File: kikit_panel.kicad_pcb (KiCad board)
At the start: 4 copper layers, 56 x 47 mm, 297 parts, among them J1 Conn_01x01, J10 Conn_01x01, J11 Conn_01x01, J12 Conn_01x01, J13 Conn_01x01, J14 Conn_01x01, J15 Conn_01x01, J16 Conn_01x01, J17 Conn_Coaxial, J2 Conn_01x01, J3 Conn_01x01, J4 Conn_01x01, J5 Conn_01x01, J6 Conn_01x01, J7 Conn_01x01, J8 Conn_01x01, J9 Conn_01x01, U1 SX1280IMLTRT, U2 2450FM07D0034T, X1 52.000 MHz

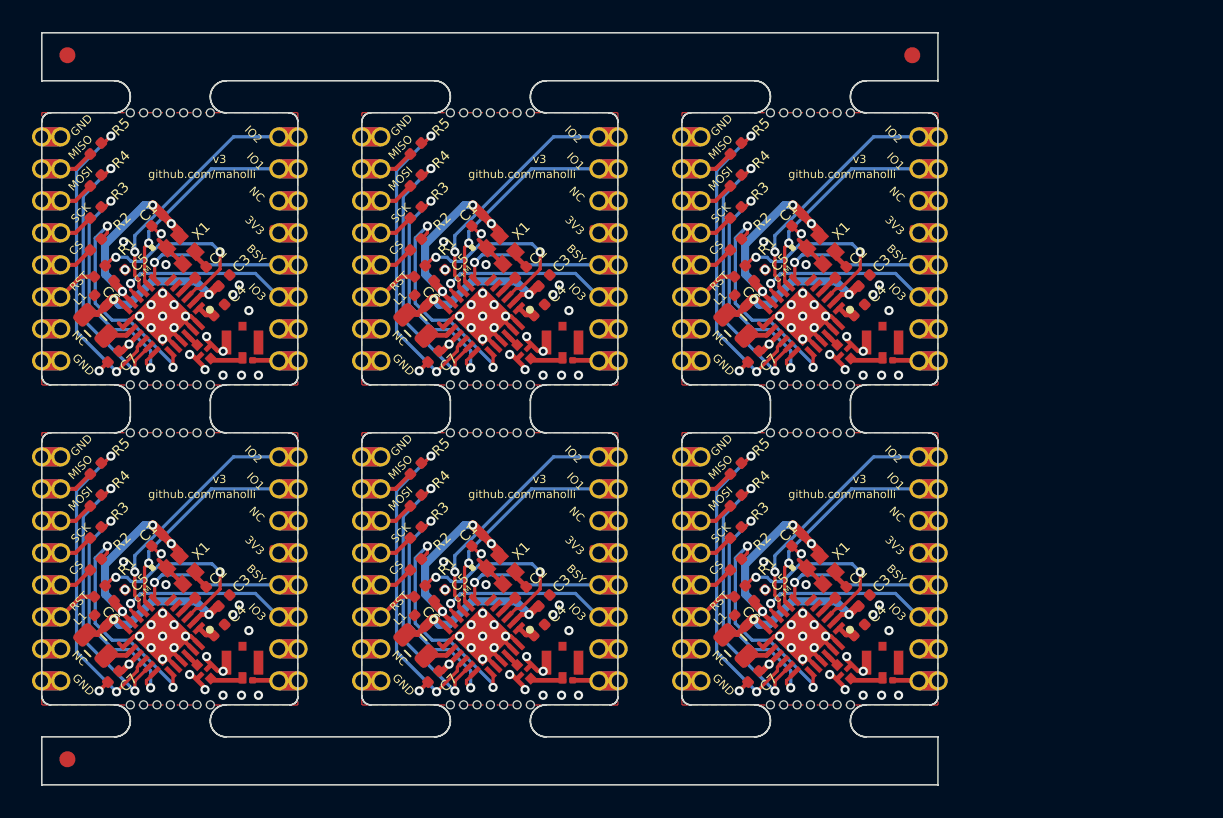
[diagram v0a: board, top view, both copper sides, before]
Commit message: panelized just in case
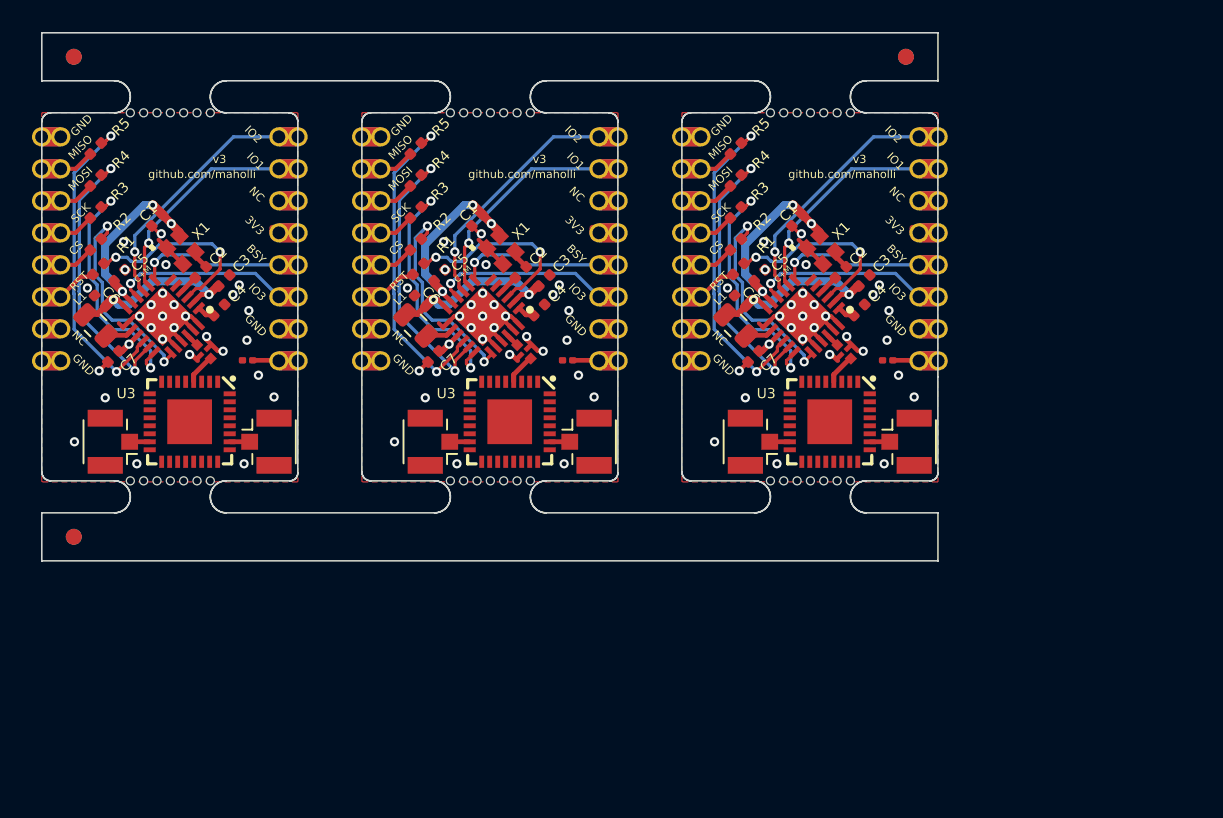
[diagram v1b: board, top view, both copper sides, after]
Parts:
- removed the C1 at (62.2, 46.7)
- removed the C1 at (42.2, 46.7)
- removed the C1 at (22.2, 46.7)
- removed the C2 at (64.9, 50.0)
- removed the C2 at (24.9, 50.0)
- removed the C2 at (44.9, 50.0)
- removed the C3 at (66.4, 50.5)
- removed the C3 at (46.4, 50.5)
- removed the C3 at (26.4, 50.5)
- removed the C4 at (26.1, 52.3)
- removed the C4 at (46.1, 52.3)
- removed the C4 at (66.1, 52.3)
- removed the C5 at (59.9, 50.2)
- removed the C5 at (39.9, 50.2)
- removed the C5 at (19.9, 50.2)
- removed the C6 at (38.6, 51.7)
- removed the C6 at (18.6, 51.7)
- removed the C6 at (18.6, 31.7)
- removed the C6 at (58.6, 31.7)
- removed the C6 at (58.6, 51.7)
- removed the C6 at (38.6, 31.7)
- removed the C7 at (59.5, 55.2)
- removed the C7 at (39.5, 55.2)
- removed the C7 at (19.5, 55.2)
- removed the J1 at (35.0, 41.5)
- removed the J1 at (15.0, 41.5)
- removed the J1 at (55.0, 41.5)
- removed the J10 at (31.0, 53.5)
- removed the J10 at (71.0, 53.5)
- removed the J10 at (51.0, 53.5)
- removed the J11 at (51.0, 51.5)
- removed the J11 at (31.0, 51.5)
- removed the J11 at (71.0, 51.5)
- removed the J12 at (51.0, 49.5)
- removed the J12 at (71.0, 49.5)
- removed the J12 at (31.0, 49.5)
- removed the J13 at (31.0, 47.5)
- removed the J13 at (51.0, 47.5)
- removed the J13 at (71.0, 47.5)
- removed the J14 at (51.0, 45.5)
- removed the J14 at (71.0, 45.5)
- removed the J14 at (31.0, 45.5)
- removed the J15 at (51.0, 43.5)
- removed the J15 at (71.0, 43.5)
- removed the J15 at (31.0, 43.5)
- removed the J16 at (31.0, 41.5)
- removed the J16 at (51.0, 41.5)
- removed the J16 at (71.0, 41.5)
- removed the J17 at (27.5, 34.4)
- removed the J17 at (27.5, 54.4)
- removed the J17 at (47.5, 34.4)
- removed the J17 at (67.5, 34.4)
- removed the J17 at (47.5, 54.4)
- removed the J17 at (67.5, 54.4)
- removed the J2 at (15.0, 43.5)
- removed the J2 at (35.0, 43.5)
- removed the J2 at (55.0, 43.5)
- removed the J3 at (55.0, 45.5)
- removed the J3 at (35.0, 45.5)
- removed the J3 at (15.0, 45.5)
- removed the J4 at (15.0, 47.5)
- removed the J4 at (35.0, 47.5)
- removed the J4 at (55.0, 47.5)
- removed the J5 at (55.0, 49.5)
- removed the J5 at (35.0, 49.5)
- removed the J5 at (15.0, 49.5)
- removed the J6 at (35.0, 51.5)
- removed the J6 at (15.0, 51.5)
- removed the J6 at (55.0, 51.5)
- removed the J7 at (55.0, 53.5)
- removed the J7 at (15.0, 53.5)
- removed the J7 at (35.0, 53.5)
- removed the J8 at (35.0, 55.5)
- removed the J8 at (15.0, 55.5)
- removed the J8 at (55.0, 55.5)
- removed the J9 at (51.0, 55.5)
- removed the J9 at (31.0, 55.5)
- removed the J9 at (71.0, 55.5)
- removed the L1 at (38.4, 53.3)
- removed the L1 at (58.4, 53.3)
- removed the L1 at (18.4, 53.3)
- removed the R1 at (38.6, 49.9)
- removed the R1 at (58.6, 29.9)
- removed the R1 at (58.6, 49.9)
- removed the R1 at (38.6, 29.9)
- removed the R1 at (18.6, 29.9)
- removed the R1 at (18.6, 49.9)
- removed the R2 at (18.4, 48.2)
- removed the R2 at (58.4, 48.2)
- removed the R2 at (38.4, 48.2)
- removed the R3 at (58.4, 46.2)
- removed the R3 at (18.4, 46.2)
- removed the R3 at (38.4, 46.2)
- removed the R4 at (58.4, 44.2)
- removed the R4 at (18.4, 44.2)
- removed the R4 at (38.4, 44.2)
- removed the R5 at (18.4, 42.2)
- removed the R5 at (38.4, 42.2)
- removed the R5 at (58.4, 42.2)
- removed the R6 at (67.9, 55.5)
- removed the R6 at (27.9, 55.5)
- removed the R6 at (47.9, 55.5)
- removed the REF** at (62.2, 40.0)
- removed the REF** at (63.0, 37.0)
- removed the REF** at (60.5, 57.0)
- removed the REF** at (23.0, 40.0)
- removed the REF** at (43.9, 40.0)
- removed the REF** at (43.0, 57.0)
- removed the REF** at (41.4, 40.0)
- removed the REF** at (61.4, 37.0)
- removed the REF** at (23.9, 40.0)
- removed the REF** at (63.9, 40.0)
- removed the REF** at (40.5, 40.0)
- removed the REF** at (63.0, 40.0)
- removed the REF** at (22.2, 37.0)
- removed the REF** at (25.5, 57.0)
- removed the REF** at (20.5, 40.0)
- removed the REF** at (65.5, 40.0)
- removed the REF** at (61.4, 57.0)
- removed the REF** at (62.2, 37.0)
- removed the REF** at (24.7, 40.0)
- removed the REF** at (23.9, 37.0)
- removed the REF** at (44.7, 57.0)
- removed the REF** at (23.9, 57.0)
- removed the REF** at (24.7, 37.0)
- removed the REF** at (45.5, 37.0)
- removed the REF** at (60.5, 37.0)
- removed the REF** at (63.0, 57.0)
- removed the REF** at (42.2, 57.0)
- removed the REF** at (43.0, 40.0)
- removed the REF** at (64.7, 37.0)
- removed the REF** at (23.0, 37.0)
- removed the REF** at (25.5, 37.0)
- removed the REF** at (64.7, 40.0)
- removed the REF** at (64.7, 57.0)
- removed the REF** at (21.4, 40.0)
- removed the REF** at (24.7, 57.0)
- removed the REF** at (62.2, 57.0)
- removed the REF** at (20.5, 37.0)
- removed the REF** at (43.9, 57.0)
- removed the REF** at (45.5, 40.0)
- removed the REF** at (40.5, 37.0)
- removed the REF** at (25.5, 40.0)
- removed the REF** at (65.5, 57.0)
- removed the REF** at (41.4, 37.0)
- removed the REF** at (23.0, 57.0)
- removed the REF** at (40.5, 57.0)
- removed the REF** at (21.4, 57.0)
- removed the REF** at (60.5, 40.0)
- removed the REF** at (16.6, 60.4)
- removed the REF** at (65.5, 37.0)
- removed the REF** at (44.7, 40.0)
- removed the REF** at (44.7, 37.0)
- removed the REF** at (45.5, 57.0)
- removed the REF** at (61.4, 40.0)
- removed the REF** at (21.4, 37.0)
- removed the REF** at (16.6, 16.4)
- removed the REF** at (69.4, 16.4)
- removed the REF** at (63.9, 37.0)
- removed the REF** at (43.0, 37.0)
- removed the REF** at (22.2, 40.0)
- removed the REF** at (41.4, 57.0)
- removed the REF** at (22.2, 57.0)
- removed the REF** at (43.9, 37.0)
- removed the REF** at (63.9, 57.0)
- removed the REF** at (42.2, 37.0)
- removed the REF** at (20.5, 57.0)
- removed the REF** at (42.2, 40.0)
- removed the Ref** at (42.8, 44.8)
- removed the Ref** at (62.8, 44.8)
- removed the Ref** at (22.8, 44.8)
- removed the U1 at (62.6, 52.7)
- removed the U1 at (42.6, 52.7)
- removed the U1 at (22.5, 52.7)
- removed the U2 at (25.1, 54.9)
- removed the U2 at (65.1, 54.9)
- removed the U2 at (45.1, 54.9)
- removed the X1 at (63.7, 48.6)
- removed the X1 at (23.7, 48.6)
- removed the X1 at (43.7, 48.6)
- added C6: 470nF, Capacitor_SMD:C_0402_1005Metric, F.Cu at (18.6, 31.8)
- added C6: 470nF, Capacitor_SMD:C_0402_1005Metric, F.Cu at (38.6, 31.8)
- added C6: 470nF, Capacitor_SMD:C_0402_1005Metric, F.Cu at (58.6, 31.8)
- added J17: u.FL, Connector_Coaxial:U.FL_Hirose_U.FL-R-SMT-1_Vertical, F.Cu at (59.4, 40.6)
- added J17: u.FL, Connector_Coaxial:U.FL_Hirose_U.FL-R-SMT-1_Vertical, F.Cu at (39.4, 40.6)
- added J17: u.FL, Connector_Coaxial:U.FL_Hirose_U.FL-R-SMT-1_Vertical, F.Cu at (19.4, 40.6)
- added J18: u.FL, Connector_Coaxial:U.FL_Hirose_U.FL-R-SMT-1_Vertical, F.Cu at (29.0, 40.6)
- added J18: u.FL, Connector_Coaxial:U.FL_Hirose_U.FL-R-SMT-1_Vertical, F.Cu at (69.0, 40.6)
- added J18: u.FL, Connector_Coaxial:U.FL_Hirose_U.FL-R-SMT-1_Vertical, F.Cu at (49.0, 40.6)
- added R1: 1k, Resistor_SMD:R_0402_1005Metric, F.Cu at (58.5, 29.8)
- added R1: 1k, Resistor_SMD:R_0402_1005Metric, F.Cu at (38.5, 29.8)
- added R1: 1k, Resistor_SMD:R_0402_1005Metric, F.Cu at (18.5, 29.8)
- added REF**: NPTH, NPTH, F.Cu at (21.4, 43.0)
- added REF**: NPTH, NPTH, F.Cu at (61.4, 43.0)
- added REF**: NPTH, NPTH, F.Cu at (63.9, 43.0)
- added REF**: NPTH, NPTH, F.Cu at (42.2, 43.0)
- added REF**: NPTH, NPTH, F.Cu at (62.2, 43.0)
- added REF**: NPTH, NPTH, F.Cu at (64.7, 43.0)
- added REF**: Fiducial, Fiducial, F.Cu at (17.0, 16.5)
- added REF**: NPTH, NPTH, F.Cu at (41.4, 43.0)
- added REF**: NPTH, NPTH, F.Cu at (24.7, 43.0)
- added REF**: NPTH, NPTH, F.Cu at (44.7, 43.0)
- added REF**: NPTH, NPTH, F.Cu at (23.0, 43.0)
- added REF**: NPTH, NPTH, F.Cu at (22.2, 43.0)
- added REF**: NPTH, NPTH, F.Cu at (60.5, 43.0)
- added REF**: NPTH, NPTH, F.Cu at (23.9, 43.0)
- added REF**: NPTH, NPTH, F.Cu at (40.5, 43.0)
- added REF**: NPTH, NPTH, F.Cu at (45.5, 43.0)
- added REF**: Fiducial, Fiducial, F.Cu at (69.0, 16.5)
- added REF**: NPTH, NPTH, F.Cu at (20.5, 43.0)
- added REF**: NPTH, NPTH, F.Cu at (25.5, 43.0)
- added REF**: NPTH, NPTH, F.Cu at (43.0, 43.0)
- added REF**: Fiducial, Fiducial, F.Cu at (17.0, 46.5)
- added REF**: Fiducial, Fiducial, B.Cu at (17.0, 46.5)
- added REF**: Fiducial, Fiducial, B.Cu at (69.0, 16.5)
- added REF**: Fiducial, Fiducial, B.Cu at (17.0, 16.5)
- added REF**: NPTH, NPTH, F.Cu at (43.9, 43.0)
- added REF**: NPTH, NPTH, F.Cu at (65.5, 43.0)
- added REF**: NPTH, NPTH, F.Cu at (63.0, 43.0)
- added U3: EP2W+, custom-footprints:QFN32-5X5MM, F.Cu at (24.2, 39.3)
- added U3: EP2W+, custom-footprints:QFN32-5X5MM, F.Cu at (64.2, 39.3)
- added U3: EP2W+, custom-footprints:QFN32-5X5MM, F.Cu at (44.2, 39.3)
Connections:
- net Board_0-Net-(X1-Pad3) renamed Board_0-Net-(C2-Pad2)
- net Board_1-Net-(X1-Pad3) renamed Board_1-Net-(C2-Pad2)
- net Board_2-Net-(X1-Pad3) renamed Board_2-Net-(C2-Pad2)
- R6 pad 1: Board_1-Net-(J17-Pad1) -> Board_1-unconnected-(R6-Pad1)
- R6 pad 1: Board_0-Net-(J17-Pad1) -> Board_0-unconnected-(R6-Pad1)
- R6 pad 1: Board_2-Net-(J17-Pad1) -> Board_2-unconnected-(R6-Pad1)
- U2 pad 3: Board_2-Net-(J17-Pad1) -> Board_2-Net-(U2-Pad3)
- U2 pad 3: Board_0-Net-(J17-Pad1) -> Board_0-Net-(U2-Pad3)
- U2 pad 3: Board_1-Net-(J17-Pad1) -> Board_1-Net-(U2-Pad3)
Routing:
- net Board_5-+3V3: track 24.2 -> 0.00 mm, vias 4 -> 0
- net Board_4-+3V3: track 24.2 -> 0.00 mm, vias 4 -> 0
- net Board_3-+3V3: track 24.2 -> 0.00 mm, vias 4 -> 0
- net Board_5-Net-(R5-Pad2): track 20.0 -> 0.00 mm, vias 2 -> 0
- net Board_4-Net-(R5-Pad2): track 20.0 -> 0.00 mm, vias 2 -> 0
- net Board_3-Net-(R5-Pad2): track 20.0 -> 0.00 mm, vias 2 -> 0
- net Board_5-Net-(R4-Pad2): track 17.4 -> 0.00 mm, vias 2 -> 0
- net Board_4-Net-(R4-Pad2): track 17.4 -> 0.00 mm, vias 2 -> 0
- net Board_3-Net-(R4-Pad2): track 17.4 -> 0.00 mm, vias 2 -> 0
- net Board_5-SX_DIO2: track 15.3 -> 0.00 mm, vias 1 -> 0
- net Board_4-SX_DIO2: track 15.3 -> 0.00 mm, vias 1 -> 0
- net Board_3-SX_DIO2: track 15.3 -> 0.00 mm, vias 1 -> 0
- net Board_5-Net-(R3-Pad2): track 15.2 -> 0.00 mm, vias 2 -> 0
- net Board_3-Net-(R3-Pad2): track 15.2 -> 0.00 mm, vias 2 -> 0
- net Board_4-Net-(R3-Pad2): track 15.2 -> 0.00 mm, vias 2 -> 0
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- removed copper zone on F.Cu, net Board_3-GND
- removed copper zone on In1.Cu, net Board_3-GND
- removed copper zone on In2.Cu, net Board_3-GND
- removed copper zone on F.Cu, net Board_4-GND
- removed copper zone on In1.Cu, net Board_4-GND
- removed copper zone on In2.Cu, net Board_4-GND
- removed copper zone on F.Cu, net Board_5-GND
- removed copper zone on In1.Cu, net Board_5-GND
- removed copper zone on In2.Cu, net Board_5-GND
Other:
- board size 56 x 47 mm -> 56 x 33 mm

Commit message: back to single antenna
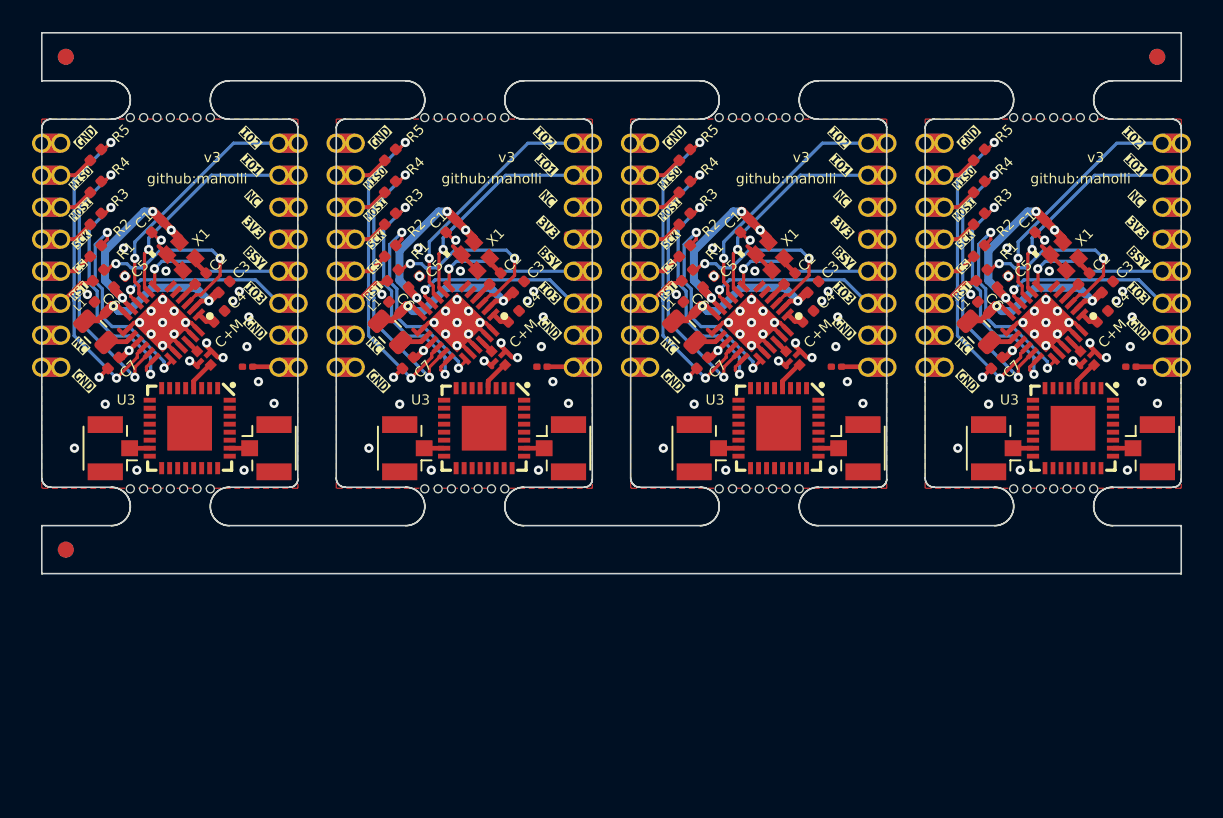
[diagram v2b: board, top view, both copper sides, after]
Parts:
- removed the C1 at (62.2, 26.7)
- removed the C1 at (22.2, 26.7)
- removed the C1 at (42.2, 26.7)
- removed the C2 at (44.9, 30.0)
- removed the C2 at (64.9, 30.0)
- removed the C2 at (24.9, 30.0)
- removed the C3 at (66.4, 30.5)
- removed the C3 at (46.4, 30.5)
- removed the C3 at (26.4, 30.5)
- removed the C4 at (26.1, 32.3)
- removed the C4 at (66.1, 32.3)
- removed the C4 at (46.1, 32.3)
- removed the C5 at (39.9, 30.2)
- removed the C5 at (59.9, 30.2)
- removed the C5 at (19.9, 30.2)
- removed the C6 at (18.6, 31.8)
- removed the C6 at (38.6, 31.8)
- removed the C6 at (58.6, 31.8)
- removed the C7 at (59.5, 35.2)
- removed the C7 at (39.5, 35.2)
- removed the C7 at (19.5, 35.2)
- removed the J1 at (15.0, 21.5)
- removed the J1 at (55.0, 21.5)
- removed the J1 at (35.0, 21.5)
- removed the J10 at (51.0, 33.5)
- removed the J10 at (31.0, 33.5)
- removed the J10 at (71.0, 33.5)
- removed the J11 at (31.0, 31.5)
- removed the J11 at (71.0, 31.5)
- removed the J11 at (51.0, 31.5)
- removed the J12 at (31.0, 29.5)
- removed the J12 at (71.0, 29.5)
- removed the J12 at (51.0, 29.5)
- removed the J13 at (51.0, 27.5)
- removed the J13 at (71.0, 27.5)
- removed the J13 at (31.0, 27.5)
- removed the J14 at (31.0, 25.5)
- removed the J14 at (71.0, 25.5)
- removed the J14 at (51.0, 25.5)
- removed the J15 at (71.0, 23.5)
- removed the J15 at (51.0, 23.5)
- removed the J15 at (31.0, 23.5)
- removed the J16 at (31.0, 21.5)
- removed the J16 at (71.0, 21.5)
- removed the J16 at (51.0, 21.5)
- removed the J17 at (59.4, 40.6)
- removed the J17 at (39.4, 40.6)
- removed the J17 at (19.4, 40.6)
- removed the J18 at (29.0, 40.6)
- removed the J18 at (69.0, 40.6)
- removed the J18 at (49.0, 40.6)
- removed the J2 at (15.0, 23.5)
- removed the J2 at (35.0, 23.5)
- removed the J2 at (55.0, 23.5)
- removed the J3 at (35.0, 25.5)
- removed the J3 at (55.0, 25.5)
- removed the J3 at (15.0, 25.5)
- removed the J4 at (35.0, 27.5)
- removed the J4 at (55.0, 27.5)
- removed the J4 at (15.0, 27.5)
- removed the J5 at (55.0, 29.5)
- removed the J5 at (15.0, 29.5)
- removed the J5 at (35.0, 29.5)
- removed the J6 at (15.0, 31.5)
- removed the J6 at (35.0, 31.5)
- removed the J6 at (55.0, 31.5)
- removed the J7 at (15.0, 33.5)
- removed the J7 at (55.0, 33.5)
- removed the J7 at (35.0, 33.5)
- removed the J8 at (55.0, 35.5)
- removed the J8 at (15.0, 35.5)
- removed the J8 at (35.0, 35.5)
- removed the J9 at (71.0, 35.5)
- removed the J9 at (31.0, 35.5)
- removed the J9 at (51.0, 35.5)
- removed the L1 at (38.4, 33.3)
- removed the L1 at (58.4, 33.3)
- removed the L1 at (18.4, 33.3)
- removed the R1 at (58.5, 29.8)
- removed the R1 at (38.5, 29.8)
- removed the R1 at (18.5, 29.8)
- removed the R2 at (38.4, 28.2)
- removed the R2 at (18.4, 28.2)
- removed the R2 at (58.4, 28.2)
- removed the R3 at (38.4, 26.2)
- removed the R3 at (58.4, 26.2)
- removed the R3 at (18.4, 26.2)
- removed the R4 at (38.4, 24.2)
- removed the R4 at (58.4, 24.2)
- removed the R4 at (18.4, 24.2)
- removed the R5 at (58.4, 22.2)
- removed the R5 at (38.4, 22.2)
- removed the R5 at (18.4, 22.2)
- removed the R6 at (47.9, 35.5)
- removed the R6 at (27.9, 35.5)
- removed the R6 at (67.9, 35.5)
- removed the REF** at (21.4, 43.0)
- removed the REF** at (65.5, 20.0)
- removed the REF** at (61.4, 43.0)
- removed the REF** at (63.9, 43.0)
- removed the REF** at (63.9, 20.0)
- removed the REF** at (42.2, 43.0)
- removed the REF** at (64.7, 20.0)
- removed the REF** at (62.2, 43.0)
- removed the REF** at (64.7, 43.0)
- removed the REF** at (61.4, 20.0)
- removed the REF** at (17.0, 16.5) (x2)
- removed the REF** at (41.4, 43.0)
- removed the REF** at (24.7, 43.0)
- removed the REF** at (22.2, 20.0)
- removed the REF** at (44.7, 43.0)
- removed the REF** at (24.7, 20.0)
- removed the REF** at (40.5, 20.0)
- removed the REF** at (23.0, 43.0)
- removed the REF** at (23.9, 20.0)
- removed the REF** at (22.2, 43.0)
- removed the REF** at (44.7, 20.0)
- removed the REF** at (45.5, 20.0)
- removed the REF** at (62.2, 20.0)
- removed the REF** at (63.0, 20.0)
- removed the REF** at (60.5, 43.0)
- removed the REF** at (23.9, 43.0)
- removed the REF** at (40.5, 43.0)
- removed the REF** at (45.5, 43.0)
- removed the REF** at (69.0, 16.5) (x2)
- removed the REF** at (41.4, 20.0)
- removed the REF** at (60.5, 20.0)
- removed the REF** at (20.5, 43.0)
- removed the REF** at (23.0, 20.0)
- removed the REF** at (43.9, 20.0)
- removed the REF** at (25.5, 43.0)
- removed the REF** at (21.4, 20.0)
- removed the REF** at (25.5, 20.0)
- removed the REF** at (43.0, 20.0)
- removed the REF** at (43.0, 43.0)
- removed the REF** at (17.0, 46.5) (x2)
- removed the REF** at (43.9, 43.0)
- removed the REF** at (65.5, 43.0)
- removed the REF** at (63.0, 43.0)
- removed the REF** at (42.2, 20.0)
- removed the REF** at (20.5, 20.0)
- removed the Ref** at (22.8, 24.8)
- removed the Ref** at (42.8, 24.8)
- removed the Ref** at (62.8, 24.8)
- removed the U1 at (42.6, 32.7)
- removed the U1 at (22.5, 32.7)
- removed the U1 at (62.6, 32.7)
- removed the U2 at (65.1, 34.9)
- removed the U2 at (25.1, 34.9)
- removed the U2 at (45.1, 34.9)
- removed the U3 at (24.2, 39.3)
- removed the U3 at (64.2, 39.3)
- removed the U3 at (44.2, 39.3)
- removed the X1 at (23.7, 28.6)
- removed the X1 at (63.7, 28.6)
- removed the X1 at (43.7, 28.6)
- added C1: 100nF, Capacitor_SMD:C_0402_1005Metric, F.Cu at (77.4, 27.1)
- added C1: 100nF, Capacitor_SMD:C_0402_1005Metric, F.Cu at (22.2, 27.1)
- added C1: 100nF, Capacitor_SMD:C_0402_1005Metric, F.Cu at (40.6, 27.1)
- added C1: 100nF, Capacitor_SMD:C_0402_1005Metric, F.Cu at (59.0, 27.1)
- added C2: 1nF, Capacitor_SMD:C_0402_1005Metric, F.Cu at (43.3, 30.4)
- added C2: 1nF, Capacitor_SMD:C_0402_1005Metric, F.Cu at (24.9, 30.4)
- added C2: 1nF, Capacitor_SMD:C_0402_1005Metric, F.Cu at (80.1, 30.4)
- added C2: 1nF, Capacitor_SMD:C_0402_1005Metric, F.Cu at (61.7, 30.4)
- added C3: 10nF, Capacitor_SMD:C_0402_1005Metric, F.Cu at (81.6, 30.9)
- added C3: 10nF, Capacitor_SMD:C_0402_1005Metric, F.Cu at (63.2, 30.9)
- added C3: 10nF, Capacitor_SMD:C_0402_1005Metric, F.Cu at (26.4, 30.9)
- added C3: 10nF, Capacitor_SMD:C_0402_1005Metric, F.Cu at (44.8, 30.9)
- added C4: 10nF, Capacitor_SMD:C_0402_1005Metric, F.Cu at (44.5, 32.7)
- added C4: 10nF, Capacitor_SMD:C_0402_1005Metric, F.Cu at (81.3, 32.7)
- added C4: 10nF, Capacitor_SMD:C_0402_1005Metric, F.Cu at (62.9, 32.7)
- added C4: 10nF, Capacitor_SMD:C_0402_1005Metric, F.Cu at (26.1, 32.7)
- added C5: 0.1uF, Capacitor_SMD:C_0402_1005Metric, F.Cu at (19.9, 30.6)
- added C5: 0.1uF, Capacitor_SMD:C_0402_1005Metric, F.Cu at (56.7, 30.6)
- added C5: 0.1uF, Capacitor_SMD:C_0402_1005Metric, F.Cu at (38.3, 30.6)
- added C5: 0.1uF, Capacitor_SMD:C_0402_1005Metric, F.Cu at (75.1, 30.6)
- added C6: 470nF, Capacitor_SMD:C_0402_1005Metric, F.Cu at (18.6, 32.2)
- added C6: 470nF, Capacitor_SMD:C_0402_1005Metric, F.Cu at (37.0, 32.2)
- added C6: 470nF, Capacitor_SMD:C_0402_1005Metric, F.Cu at (73.8, 32.2)
- added C6: 470nF, Capacitor_SMD:C_0402_1005Metric, F.Cu at (55.4, 32.2)
- added C7: 0.1uF, Capacitor_SMD:C_0402_1005Metric, F.Cu at (74.7, 35.6)
- added C7: 0.1uF, Capacitor_SMD:C_0402_1005Metric, F.Cu at (19.5, 35.6)
- added C7: 0.1uF, Capacitor_SMD:C_0402_1005Metric, F.Cu at (56.3, 35.6)
- added C7: 0.1uF, Capacitor_SMD:C_0402_1005Metric, F.Cu at (37.9, 35.6)
- added J1: Conn_01x01, custom-footprints:castellated_04mm, F.Cu at (15.0, 21.9)
- added J1: Conn_01x01, custom-footprints:castellated_04mm, F.Cu at (70.2, 21.9)
- added J1: Conn_01x01, custom-footprints:castellated_04mm, F.Cu at (33.4, 21.9)
- added J1: Conn_01x01, custom-footprints:castellated_04mm, F.Cu at (51.8, 21.9)
- added J10: Conn_01x01, custom-footprints:castellated_04mm, F.Cu at (49.4, 33.9)
- added J10: Conn_01x01, custom-footprints:castellated_04mm, F.Cu at (31.0, 33.9)
- added J10: Conn_01x01, custom-footprints:castellated_04mm, F.Cu at (67.8, 33.9)
- added J10: Conn_01x01, custom-footprints:castellated_04mm, F.Cu at (86.2, 33.9)
- added J11: Conn_01x01, custom-footprints:castellated_04mm, F.Cu at (49.4, 31.9)
- added J11: Conn_01x01, custom-footprints:castellated_04mm, F.Cu at (86.2, 31.9)
- added J11: Conn_01x01, custom-footprints:castellated_04mm, F.Cu at (67.8, 31.9)
- added J11: Conn_01x01, custom-footprints:castellated_04mm, F.Cu at (31.0, 31.9)
- added J12: Conn_01x01, custom-footprints:castellated_04mm, F.Cu at (67.8, 29.9)
- added J12: Conn_01x01, custom-footprints:castellated_04mm, F.Cu at (49.4, 29.9)
- added J12: Conn_01x01, custom-footprints:castellated_04mm, F.Cu at (31.0, 29.9)
- added J12: Conn_01x01, custom-footprints:castellated_04mm, F.Cu at (86.2, 29.9)
- added J13: Conn_01x01, custom-footprints:castellated_04mm, F.Cu at (67.8, 27.9)
- added J13: Conn_01x01, custom-footprints:castellated_04mm, F.Cu at (49.4, 27.9)
- added J13: Conn_01x01, custom-footprints:castellated_04mm, F.Cu at (31.0, 27.9)
- added J13: Conn_01x01, custom-footprints:castellated_04mm, F.Cu at (86.2, 27.9)
- added J14: Conn_01x01, custom-footprints:castellated_04mm, F.Cu at (49.4, 25.9)
- added J14: Conn_01x01, custom-footprints:castellated_04mm, F.Cu at (67.8, 25.9)
- added J14: Conn_01x01, custom-footprints:castellated_04mm, F.Cu at (86.2, 25.9)
- added J14: Conn_01x01, custom-footprints:castellated_04mm, F.Cu at (31.0, 25.9)
- added J15: Conn_01x01, custom-footprints:castellated_04mm, F.Cu at (86.2, 23.9)
- added J15: Conn_01x01, custom-footprints:castellated_04mm, F.Cu at (49.4, 23.9)
- added J15: Conn_01x01, custom-footprints:castellated_04mm, F.Cu at (67.8, 23.9)
- added J15: Conn_01x01, custom-footprints:castellated_04mm, F.Cu at (31.0, 23.9)
- added J16: Conn_01x01, custom-footprints:castellated_04mm, F.Cu at (67.8, 21.9)
- added J16: Conn_01x01, custom-footprints:castellated_04mm, F.Cu at (86.2, 21.9)
- added J16: Conn_01x01, custom-footprints:castellated_04mm, F.Cu at (49.4, 21.9)
- added J16: Conn_01x01, custom-footprints:castellated_04mm, F.Cu at (31.0, 21.9)
- added J17: u.FL, Connector_Coaxial:U.FL_Hirose_U.FL-R-SMT-1_Vertical, F.Cu at (56.2, 41.0)
- added J17: u.FL, Connector_Coaxial:U.FL_Hirose_U.FL-R-SMT-1_Vertical, F.Cu at (37.8, 41.0)
- added J17: u.FL, Connector_Coaxial:U.FL_Hirose_U.FL-R-SMT-1_Vertical, F.Cu at (19.4, 41.0)
- added J17: u.FL, Connector_Coaxial:U.FL_Hirose_U.FL-R-SMT-1_Vertical, F.Cu at (74.6, 41.0)
- added J18: u.FL, Connector_Coaxial:U.FL_Hirose_U.FL-R-SMT-1_Vertical, F.Cu at (47.4, 41.0)
- added J18: u.FL, Connector_Coaxial:U.FL_Hirose_U.FL-R-SMT-1_Vertical, F.Cu at (84.2, 41.0)
- added J18: u.FL, Connector_Coaxial:U.FL_Hirose_U.FL-R-SMT-1_Vertical, F.Cu at (29.0, 41.0)
- added J18: u.FL, Connector_Coaxial:U.FL_Hirose_U.FL-R-SMT-1_Vertical, F.Cu at (65.8, 41.0)
- added J2: Conn_01x01, custom-footprints:castellated_04mm, F.Cu at (51.8, 23.9)
- added J2: Conn_01x01, custom-footprints:castellated_04mm, F.Cu at (33.4, 23.9)
- added J2: Conn_01x01, custom-footprints:castellated_04mm, F.Cu at (70.2, 23.9)
- added J2: Conn_01x01, custom-footprints:castellated_04mm, F.Cu at (15.0, 23.9)
- added J3: Conn_01x01, custom-footprints:castellated_04mm, F.Cu at (15.0, 25.9)
- added J3: Conn_01x01, custom-footprints:castellated_04mm, F.Cu at (33.4, 25.9)
- added J3: Conn_01x01, custom-footprints:castellated_04mm, F.Cu at (70.2, 25.9)
- added J3: Conn_01x01, custom-footprints:castellated_04mm, F.Cu at (51.8, 25.9)
- added J4: Conn_01x01, custom-footprints:castellated_04mm, F.Cu at (70.2, 27.9)
- added J4: Conn_01x01, custom-footprints:castellated_04mm, F.Cu at (33.4, 27.9)
- added J4: Conn_01x01, custom-footprints:castellated_04mm, F.Cu at (15.0, 27.9)
- added J4: Conn_01x01, custom-footprints:castellated_04mm, F.Cu at (51.8, 27.9)
- added J5: Conn_01x01, custom-footprints:castellated_04mm, F.Cu at (70.2, 29.9)
- added J5: Conn_01x01, custom-footprints:castellated_04mm, F.Cu at (33.4, 29.9)
- added J5: Conn_01x01, custom-footprints:castellated_04mm, F.Cu at (51.8, 29.9)
- added J5: Conn_01x01, custom-footprints:castellated_04mm, F.Cu at (15.0, 29.9)
- added J6: Conn_01x01, custom-footprints:castellated_04mm, F.Cu at (51.8, 31.9)
- added J6: Conn_01x01, custom-footprints:castellated_04mm, F.Cu at (33.4, 31.9)
- added J6: Conn_01x01, custom-footprints:castellated_04mm, F.Cu at (15.0, 31.9)
- added J6: Conn_01x01, custom-footprints:castellated_04mm, F.Cu at (70.2, 31.9)
- added J7: Conn_01x01, custom-footprints:castellated_04mm, F.Cu at (15.0, 33.9)
- added J7: Conn_01x01, custom-footprints:castellated_04mm, F.Cu at (70.2, 33.9)
- added J7: Conn_01x01, custom-footprints:castellated_04mm, F.Cu at (51.8, 33.9)
- added J7: Conn_01x01, custom-footprints:castellated_04mm, F.Cu at (33.4, 33.9)
- added J8: Conn_01x01, custom-footprints:castellated_04mm, F.Cu at (33.4, 35.9)
- added J8: Conn_01x01, custom-footprints:castellated_04mm, F.Cu at (70.2, 35.9)
- added J8: Conn_01x01, custom-footprints:castellated_04mm, F.Cu at (15.0, 35.9)
- added J8: Conn_01x01, custom-footprints:castellated_04mm, F.Cu at (51.8, 35.9)
- added J9: Conn_01x01, custom-footprints:castellated_04mm, F.Cu at (31.0, 35.9)
- added J9: Conn_01x01, custom-footprints:castellated_04mm, F.Cu at (86.2, 35.9)
- added J9: Conn_01x01, custom-footprints:castellated_04mm, F.Cu at (49.4, 35.9)
- added J9: Conn_01x01, custom-footprints:castellated_04mm, F.Cu at (67.8, 35.9)
- added L1: 15uH, Inductor_SMD:L_0805_2012Metric, F.Cu at (55.2, 33.7)
- added L1: 15uH, Inductor_SMD:L_0805_2012Metric, F.Cu at (73.6, 33.7)
- added L1: 15uH, Inductor_SMD:L_0805_2012Metric, F.Cu at (18.4, 33.7)
- added L1: 15uH, Inductor_SMD:L_0805_2012Metric, F.Cu at (36.8, 33.7)
- added R1: 1k, Resistor_SMD:R_0402_1005Metric, F.Cu at (18.5, 30.2)
- added R1: 1k, Resistor_SMD:R_0402_1005Metric, F.Cu at (36.9, 30.2)
- added R1: 1k, Resistor_SMD:R_0402_1005Metric, F.Cu at (73.7, 30.2)
- added R1: 1k, Resistor_SMD:R_0402_1005Metric, F.Cu at (55.3, 30.2)
- added R2: 1k, Resistor_SMD:R_0402_1005Metric, F.Cu at (55.2, 28.6)
- added R2: 1k, Resistor_SMD:R_0402_1005Metric, F.Cu at (36.8, 28.6)
- added R2: 1k, Resistor_SMD:R_0402_1005Metric, F.Cu at (73.6, 28.6)
- added R2: 1k, Resistor_SMD:R_0402_1005Metric, F.Cu at (18.4, 28.6)
- added R3: 1k, Resistor_SMD:R_0402_1005Metric, F.Cu at (55.2, 26.6)
- added R3: 1k, Resistor_SMD:R_0402_1005Metric, F.Cu at (73.6, 26.6)
- added R3: 1k, Resistor_SMD:R_0402_1005Metric, F.Cu at (18.4, 26.6)
- added R3: 1k, Resistor_SMD:R_0402_1005Metric, F.Cu at (36.8, 26.6)
- added R4: 1k, Resistor_SMD:R_0402_1005Metric, F.Cu at (73.6, 24.6)
- added R4: 1k, Resistor_SMD:R_0402_1005Metric, F.Cu at (55.2, 24.6)
- added R4: 1k, Resistor_SMD:R_0402_1005Metric, F.Cu at (36.8, 24.6)
- added R4: 1k, Resistor_SMD:R_0402_1005Metric, F.Cu at (18.4, 24.6)
- added R5: 1k, Resistor_SMD:R_0402_1005Metric, F.Cu at (36.8, 22.6)
- added R5: 1k, Resistor_SMD:R_0402_1005Metric, F.Cu at (73.6, 22.6)
- added R5: 1k, Resistor_SMD:R_0402_1005Metric, F.Cu at (18.4, 22.6)
- added R5: 1k, Resistor_SMD:R_0402_1005Metric, F.Cu at (55.2, 22.6)
- added R6: 0, Resistor_SMD:R_0201_0603Metric, F.Cu at (83.1, 35.9)
- added R6: 0, Resistor_SMD:R_0201_0603Metric, F.Cu at (46.3, 35.9)
- added R6: 0, Resistor_SMD:R_0201_0603Metric, F.Cu at (27.9, 35.9)
- added R6: 0, Resistor_SMD:R_0201_0603Metric, F.Cu at (64.7, 35.9)
- added REF**: NPTH, NPTH, F.Cu at (57.3, 20.3)
- added REF**: NPTH, NPTH, F.Cu at (77.4, 20.3)
- added REF**: NPTH, NPTH, F.Cu at (38.9, 20.3)
- added REF**: NPTH, NPTH, F.Cu at (79.9, 43.5)
- added REF**: NPTH, NPTH, F.Cu at (78.2, 20.3)
- added REF**: NPTH, NPTH, F.Cu at (79.1, 20.3)
- added REF**: NPTH, NPTH, F.Cu at (60.7, 43.5)
- added REF**: NPTH, NPTH, F.Cu at (61.5, 43.5)
- added REF**: NPTH, NPTH, F.Cu at (76.6, 20.3)
- added REF**: NPTH, NPTH, F.Cu at (78.2, 43.5)
- added REF**: NPTH, NPTH, F.Cu at (20.5, 20.3)
- added REF**: NPTH, NPTH, F.Cu at (43.1, 20.3)
- added REF**: NPTH, NPTH, F.Cu at (61.5, 20.3)
- added REF**: NPTH, NPTH, F.Cu at (41.4, 43.5)
- added REF**: NPTH, NPTH, F.Cu at (58.2, 43.5)
- added REF**: NPTH, NPTH, F.Cu at (59.0, 43.5)
- added REF**: Fiducial, Fiducial, F.Cu at (16.5, 47.3)
- added REF**: NPTH, NPTH, F.Cu at (22.2, 43.5)
- added REF**: NPTH, NPTH, F.Cu at (42.3, 43.5)
- added REF**: NPTH, NPTH, F.Cu at (22.2, 20.3)
- added REF**: NPTH, NPTH, F.Cu at (79.1, 43.5)
- added REF**: NPTH, NPTH, F.Cu at (59.8, 20.3)
- added REF**: NPTH, NPTH, F.Cu at (80.7, 43.5)
- added REF**: NPTH, NPTH, F.Cu at (62.3, 43.5)
- added REF**: NPTH, NPTH, F.Cu at (43.9, 20.3)
- added REF**: NPTH, NPTH, F.Cu at (23.9, 43.5)
- added REF**: NPTH, NPTH, F.Cu at (59.8, 43.5)
- added REF**: NPTH, NPTH, F.Cu at (38.9, 43.5)
- added REF**: NPTH, NPTH, F.Cu at (40.6, 43.5)
- added REF**: NPTH, NPTH, F.Cu at (77.4, 43.5)
- added REF**: NPTH, NPTH, F.Cu at (75.7, 20.3)
- added REF**: NPTH, NPTH, F.Cu at (58.2, 20.3)
- added REF**: NPTH, NPTH, F.Cu at (43.1, 43.5)
- added REF**: NPTH, NPTH, F.Cu at (20.5, 43.5)
- added REF**: Fiducial, Fiducial, F.Cu at (84.7, 16.5)
- added REF**: NPTH, NPTH, F.Cu at (40.6, 20.3)
- added REF**: NPTH, NPTH, F.Cu at (25.5, 20.3)
- added REF**: NPTH, NPTH, F.Cu at (75.7, 43.5)
- added REF**: NPTH, NPTH, F.Cu at (60.7, 20.3)
- added REF**: NPTH, NPTH, F.Cu at (24.7, 20.3)
- added REF**: NPTH, NPTH, F.Cu at (59.0, 20.3)
- added REF**: NPTH, NPTH, F.Cu at (21.4, 43.5)
- added REF**: NPTH, NPTH, F.Cu at (57.3, 43.5)
- added REF**: NPTH, NPTH, F.Cu at (41.4, 20.3)
- added REF**: NPTH, NPTH, F.Cu at (79.9, 20.3)
- added REF**: NPTH, NPTH, F.Cu at (80.7, 20.3)
- added REF**: NPTH, NPTH, F.Cu at (42.3, 20.3)
- added REF**: NPTH, NPTH, F.Cu at (43.9, 43.5)
- added REF**: NPTH, NPTH, F.Cu at (76.6, 43.5)
- added REF**: NPTH, NPTH, F.Cu at (21.4, 20.3)
- added REF**: NPTH, NPTH, F.Cu at (23.9, 20.3)
- added REF**: NPTH, NPTH, F.Cu at (39.8, 20.3)
- added REF**: NPTH, NPTH, F.Cu at (39.8, 43.5)
- added REF**: NPTH, NPTH, F.Cu at (23.0, 43.5)
- added REF**: NPTH, NPTH, F.Cu at (25.5, 43.5)
- added REF**: NPTH, NPTH, F.Cu at (23.0, 20.3)
- added REF**: Fiducial, Fiducial, B.Cu at (16.5, 47.3)
- added REF**: Fiducial, Fiducial, B.Cu at (84.7, 16.5)
- added REF**: Fiducial, Fiducial, B.Cu at (16.5, 16.5)
- added REF**: Fiducial, Fiducial, F.Cu at (16.5, 16.5)
- added REF**: NPTH, NPTH, F.Cu at (62.3, 20.3)
- added REF**: NPTH, NPTH, F.Cu at (24.7, 43.5)
- added Ref**: Val**, custom-footprints:holliday, F.Cu at (78.0, 25.2)
- added Ref**: Val**, custom-footprints:holliday, F.Cu at (41.2, 25.2)
- added Ref**: Val**, custom-footprints:holliday, F.Cu at (22.8, 25.2)
- added Ref**: Val**, custom-footprints:holliday, F.Cu at (59.6, 25.2)
- added U1: SX1280IMLTRT, custom-footprints:QFN50P400X400X80-25N-D, F.Cu at (77.8, 33.1)
- added U1: SX1280IMLTRT, custom-footprints:QFN50P400X400X80-25N-D, F.Cu at (59.4, 33.1)
- added U1: SX1280IMLTRT, custom-footprints:QFN50P400X400X80-25N-D, F.Cu at (22.5, 33.1)
- added U1: SX1280IMLTRT, custom-footprints:QFN50P400X400X80-25N-D, F.Cu at (41.0, 33.1)
- added U2: 2450FM07D0034T, custom-footprints:2450FM07D0034T, F.Cu at (43.5, 35.3)
- added U2: 2450FM07D0034T, custom-footprints:2450FM07D0034T, F.Cu at (61.9, 35.3)
- added U2: 2450FM07D0034T, custom-footprints:2450FM07D0034T, F.Cu at (80.3, 35.3)
- added U2: 2450FM07D0034T, custom-footprints:2450FM07D0034T, F.Cu at (25.1, 35.3)
- added U3: EP2W+, custom-footprints:QFN32-5X5MM, F.Cu at (79.4, 39.7)
- added U3: EP2W+, custom-footprints:QFN32-5X5MM, F.Cu at (61.0, 39.7)
- added U3: EP2W+, custom-footprints:QFN32-5X5MM, F.Cu at (42.6, 39.7)
- added U3: EP2W+, custom-footprints:QFN32-5X5MM, F.Cu at (24.2, 39.7)
- added X1: 52.000 MHz, Crystal:Crystal_SMD_2016-4Pin_2.0x1.6mm, F.Cu at (42.1, 29.0)
- added X1: 52.000 MHz, Crystal:Crystal_SMD_2016-4Pin_2.0x1.6mm, F.Cu at (23.7, 29.0)
- added X1: 52.000 MHz, Crystal:Crystal_SMD_2016-4Pin_2.0x1.6mm, F.Cu at (78.9, 29.0)
- added X1: 52.000 MHz, Crystal:Crystal_SMD_2016-4Pin_2.0x1.6mm, F.Cu at (60.5, 29.0)
- added kibuzzard-62D5B0F3: G***, kibuzzard-62D5B0F3, F.Cu at (65.1, 29.1)
- added kibuzzard-62D5B0F3: G***, kibuzzard-62D5B0F3, F.Cu at (83.5, 29.1)
- added kibuzzard-62D5B0F3: G***, kibuzzard-62D5B0F3, F.Cu at (28.3, 29.1)
- added kibuzzard-62D5B0F3: G***, kibuzzard-62D5B0F3, F.Cu at (46.7, 29.1)
- added kibuzzard-62D5B0FF: G***, kibuzzard-62D5B0FF, F.Cu at (46.6, 27.2)
- added kibuzzard-62D5B0FF: G***, kibuzzard-62D5B0FF, F.Cu at (28.2, 27.2)
- added kibuzzard-62D5B0FF: G***, kibuzzard-62D5B0FF, F.Cu at (65.0, 27.2)
- added kibuzzard-62D5B0FF: G***, kibuzzard-62D5B0FF, F.Cu at (83.4, 27.2)
- added kibuzzard-62D5B106: G***, kibuzzard-62D5B106, F.Cu at (17.4, 34.6)
- added kibuzzard-62D5B106: G***, kibuzzard-62D5B106, F.Cu at (28.2, 25.4)
- added kibuzzard-62D5B106: G***, kibuzzard-62D5B106, F.Cu at (54.2, 34.6)
- added kibuzzard-62D5B106: G***, kibuzzard-62D5B106, F.Cu at (65.0, 25.4)
- added kibuzzard-62D5B106: G***, kibuzzard-62D5B106, F.Cu at (35.8, 34.6)
- added kibuzzard-62D5B106: G***, kibuzzard-62D5B106, F.Cu at (46.6, 25.4)
- added kibuzzard-62D5B106: G***, kibuzzard-62D5B106, F.Cu at (83.4, 25.4)
- added kibuzzard-62D5B106: G***, kibuzzard-62D5B106, F.Cu at (72.6, 34.6)
- added kibuzzard-62D5B10B: G***, kibuzzard-62D5B10B, F.Cu at (28.1, 23.3)
- added kibuzzard-62D5B10B: G***, kibuzzard-62D5B10B, F.Cu at (64.9, 23.3)
- added kibuzzard-62D5B10B: G***, kibuzzard-62D5B10B, F.Cu at (83.3, 23.3)
- added kibuzzard-62D5B10B: G***, kibuzzard-62D5B10B, F.Cu at (46.5, 23.3)
- added kibuzzard-62D5B111: G***, kibuzzard-62D5B111, F.Cu at (46.4, 21.6)
- added kibuzzard-62D5B111: G***, kibuzzard-62D5B111, F.Cu at (28.0, 21.6)
- added kibuzzard-62D5B111: G***, kibuzzard-62D5B111, F.Cu at (64.8, 21.6)
- added kibuzzard-62D5B111: G***, kibuzzard-62D5B111, F.Cu at (83.2, 21.6)
- added kibuzzard-62D5B116: G***, kibuzzard-62D5B116, F.Cu at (83.5, 33.5)
- added kibuzzard-62D5B116: G***, kibuzzard-62D5B116, F.Cu at (46.7, 33.5)
- added kibuzzard-62D5B116: G***, kibuzzard-62D5B116, F.Cu at (54.5, 21.5)
- added kibuzzard-62D5B116: G***, kibuzzard-62D5B116, F.Cu at (36.1, 21.5)
- added kibuzzard-62D5B116: G***, kibuzzard-62D5B116, F.Cu at (65.1, 33.5)
- added kibuzzard-62D5B116: G***, kibuzzard-62D5B116, F.Cu at (72.8, 36.8)
- added kibuzzard-62D5B116: G***, kibuzzard-62D5B116, F.Cu at (28.3, 33.5)
- added kibuzzard-62D5B116: G***, kibuzzard-62D5B116, F.Cu at (17.7, 21.5)
- added kibuzzard-62D5B116: G***, kibuzzard-62D5B116, F.Cu at (36.0, 36.8)
- added kibuzzard-62D5B116: G***, kibuzzard-62D5B116, F.Cu at (72.9, 21.5)
- added kibuzzard-62D5B116: G***, kibuzzard-62D5B116, F.Cu at (54.4, 36.8)
- added kibuzzard-62D5B116: G***, kibuzzard-62D5B116, F.Cu at (17.6, 36.8)
- added kibuzzard-62D5B11D: G***, kibuzzard-62D5B11D, F.Cu at (28.3, 31.3)
- added kibuzzard-62D5B11D: G***, kibuzzard-62D5B11D, F.Cu at (46.7, 31.3)
- added kibuzzard-62D5B11D: G***, kibuzzard-62D5B11D, F.Cu at (65.1, 31.3)
- added kibuzzard-62D5B11D: G***, kibuzzard-62D5B11D, F.Cu at (83.5, 31.3)
- added kibuzzard-62D5B296: G***, kibuzzard-62D5B296, F.Cu at (72.6, 29.6)
- added kibuzzard-62D5B296: G***, kibuzzard-62D5B296, F.Cu at (35.8, 29.6)
- added kibuzzard-62D5B296: G***, kibuzzard-62D5B296, F.Cu at (17.4, 29.6)
- added kibuzzard-62D5B296: G***, kibuzzard-62D5B296, F.Cu at (54.2, 29.6)
- added kibuzzard-62D5B29B: G***, kibuzzard-62D5B29B, F.Cu at (54.1, 31.1)
- added kibuzzard-62D5B29B: G***, kibuzzard-62D5B29B, F.Cu at (35.7, 31.1)
- added kibuzzard-62D5B29B: G***, kibuzzard-62D5B29B, F.Cu at (17.3, 31.1)
- added kibuzzard-62D5B29B: G***, kibuzzard-62D5B29B, F.Cu at (72.5, 31.1)
- added kibuzzard-62D5B2C4: G***, kibuzzard-62D5B2C4, F.Cu at (54.3, 27.9)
- added kibuzzard-62D5B2C4: G***, kibuzzard-62D5B2C4, F.Cu at (17.5, 27.9)
- added kibuzzard-62D5B2C4: G***, kibuzzard-62D5B2C4, F.Cu at (72.7, 27.9)
- added kibuzzard-62D5B2C4: G***, kibuzzard-62D5B2C4, F.Cu at (35.9, 27.9)
- added kibuzzard-62D5B2D7: G***, kibuzzard-62D5B2D7, F.Cu at (35.8, 26.1)
- added kibuzzard-62D5B2D7: G***, kibuzzard-62D5B2D7, F.Cu at (72.6, 26.1)
- added kibuzzard-62D5B2D7: G***, kibuzzard-62D5B2D7, F.Cu at (17.4, 26.1)
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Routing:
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- added copper zone on F.Cu, net Board_3-GND
- added copper zone on In1.Cu, net Board_3-GND
- added copper zone on In2.Cu, net Board_3-GND
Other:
- board size 56 x 33 mm -> 71.2 x 33.8 mm
- board text added: "github:maholli"
- board text removed: "IO1"
- board text removed: "IO2"
- board text removed: "IO3"
- board text removed: "NC"
- board text removed: "github.com/maholli"
